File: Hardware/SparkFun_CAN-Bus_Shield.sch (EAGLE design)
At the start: 43 parts, among them Q1 16MHz, U1 USD-SOCKETNEW, U2 ARDUINO_R3_SHIELD, U3 JST_VERTICAL, U4 MCP2515, U5 MCP2551, U6 HEX_CONVERTER, X1 DB9 Plug

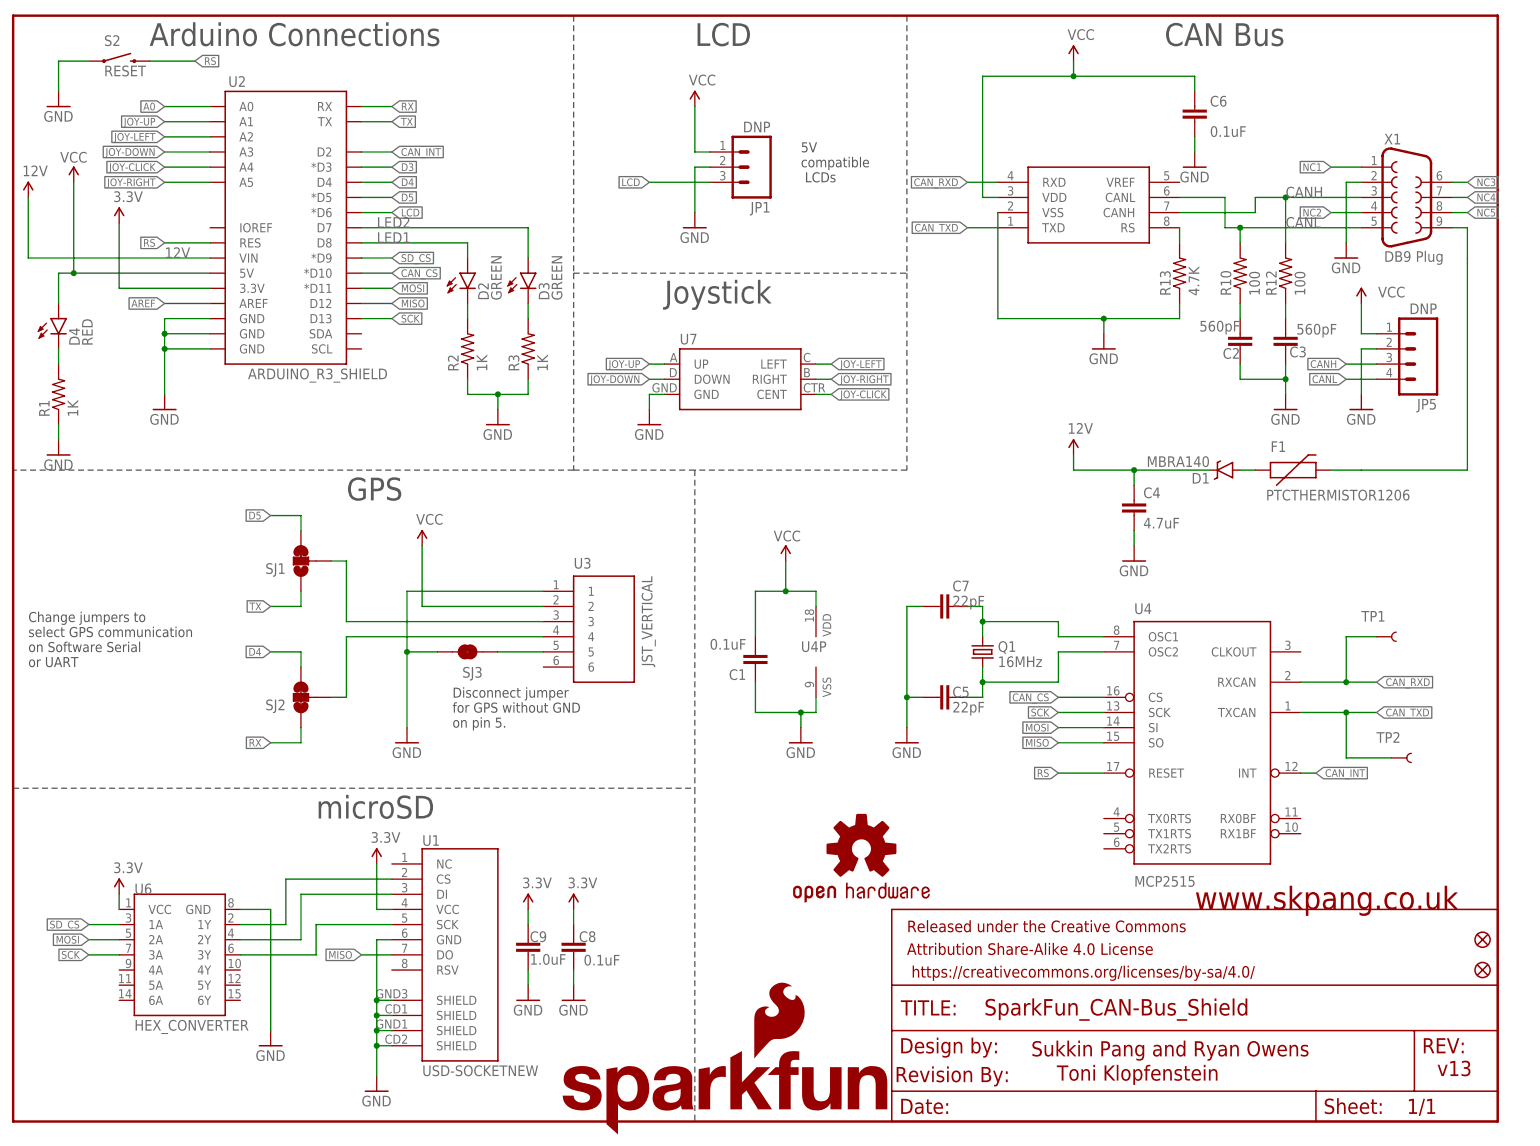
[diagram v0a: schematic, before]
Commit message: Schematic updates for QC checklist
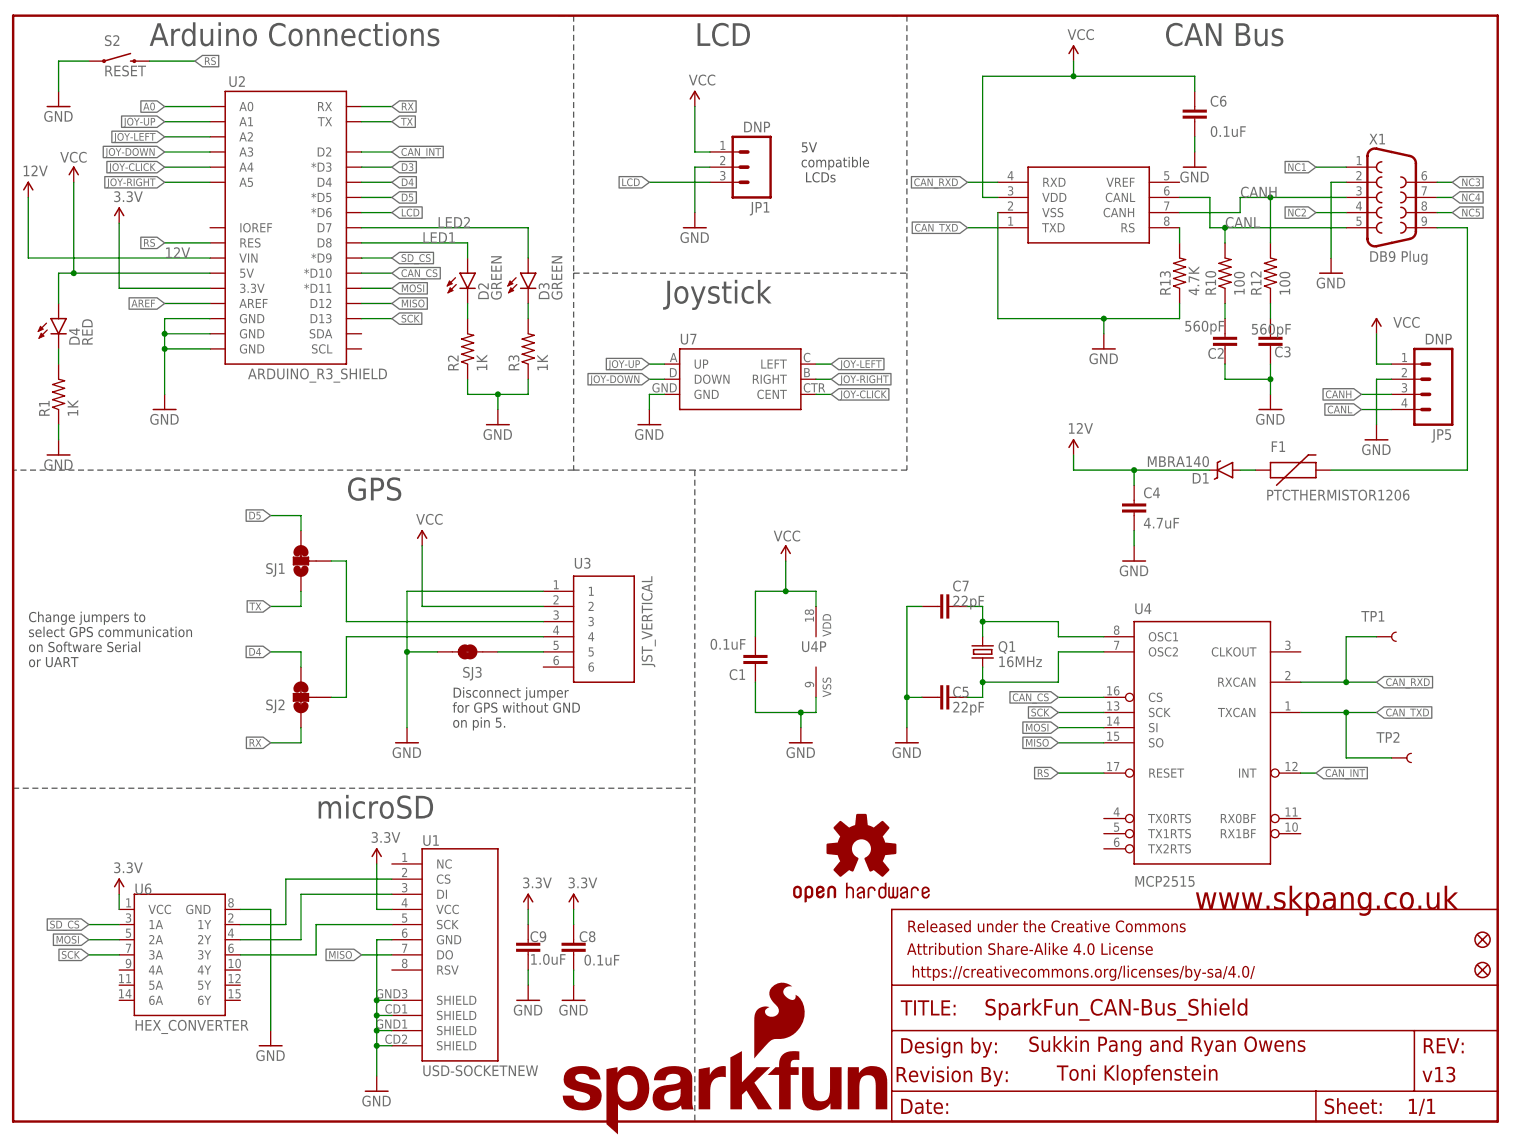
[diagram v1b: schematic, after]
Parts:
- FRAME1: value FRAME-LETTER -> (none); DESIGNER (none) -> Sukkin Pang and Ryan Owens; VERSION (none) -> v13
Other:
- note removed: "Sukkin Pang and Ryan Owens"
- note removed: "v13"
- moved on the sheet: C2, C3, JP5, R10, R12, X1

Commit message: Adding in OBDII/CAN jumpers
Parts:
- added FRAME2: (no value), SparkFun-Aesthetics:FRAME-LETTERNO_PACKAGE
- added SJ4, SJ5, SJ6: JUMPER-PAD-3-2OF3_NC_BY_TRACE_SMALL, SparkFun-Passives:JUMPER-PAD-3-2OF3_NC_BY_TRACE_SMALL
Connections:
- removed net NC4: X1.7
- new net N$2: SJ6.3, X1.5
- new net PIN2: SJ5.3, SJ6.1, X1.2
- new net PIN3: SJ4.3, SJ5.1, X1.3
- new net PIN7: SJ4.1, X1.7
- net CANH: now also SJ4.2; no longer X1.3
- net CANL: now also SJ6.2; no longer X1.5
- net GND: now also SJ5.2; no longer X1.2

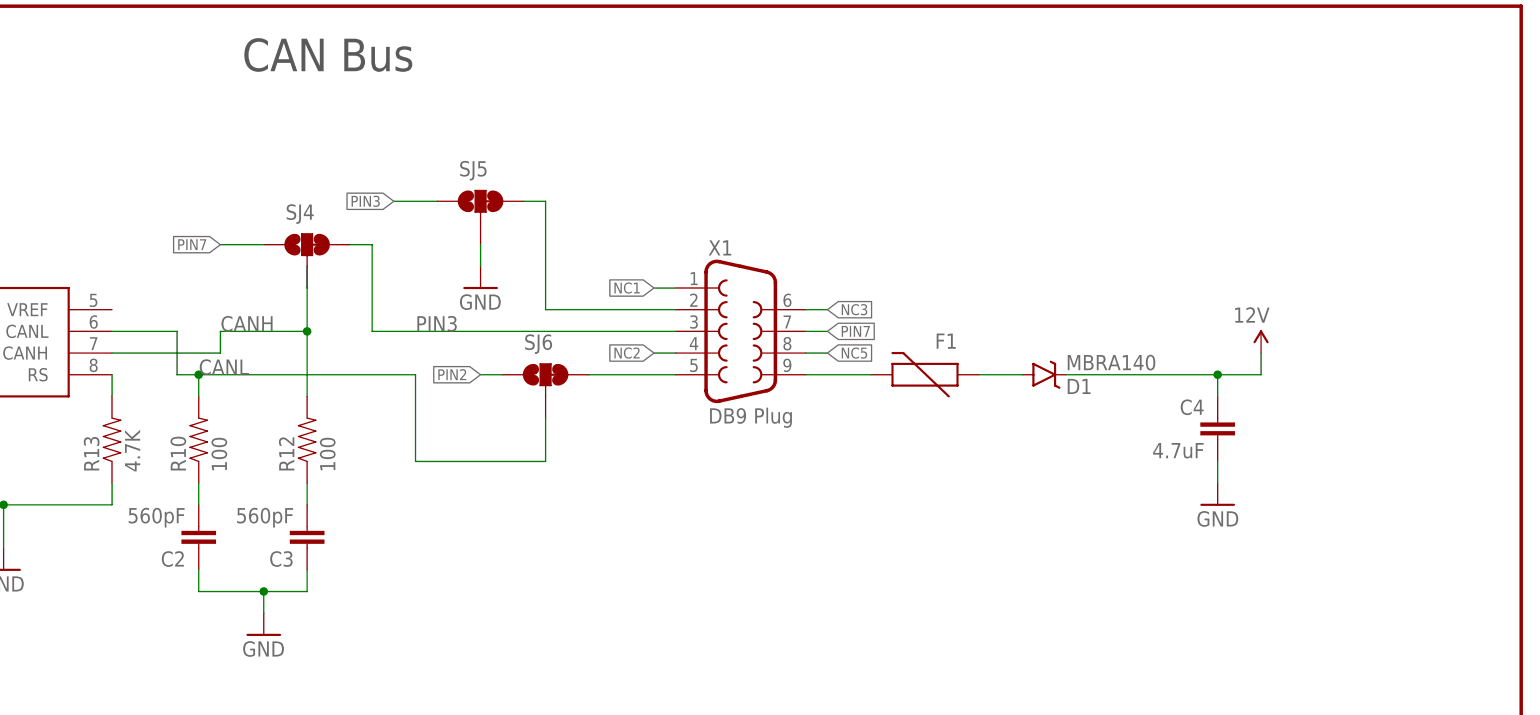
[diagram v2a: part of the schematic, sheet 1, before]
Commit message: Adding ESD protection to CAN lines
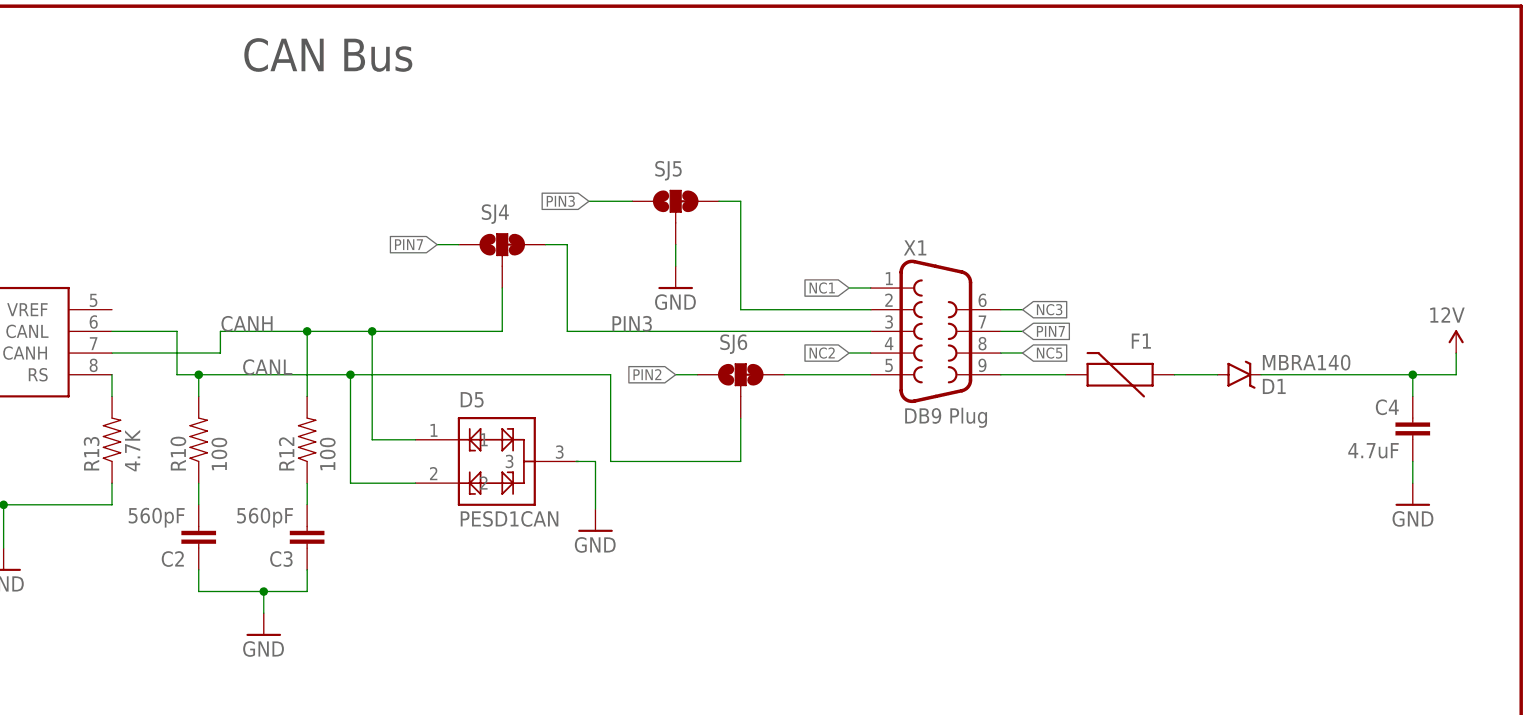
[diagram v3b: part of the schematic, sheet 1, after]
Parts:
- added D5: PESD1CAN, Testing:PESD1CAN
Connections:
- net CANH: now also D5.1
- net CANL: now also D5.2
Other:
- moved on the sheet: C4, D1, F1, SJ4, SJ5, SJ6, X1
